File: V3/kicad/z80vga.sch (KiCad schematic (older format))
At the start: 0 parts

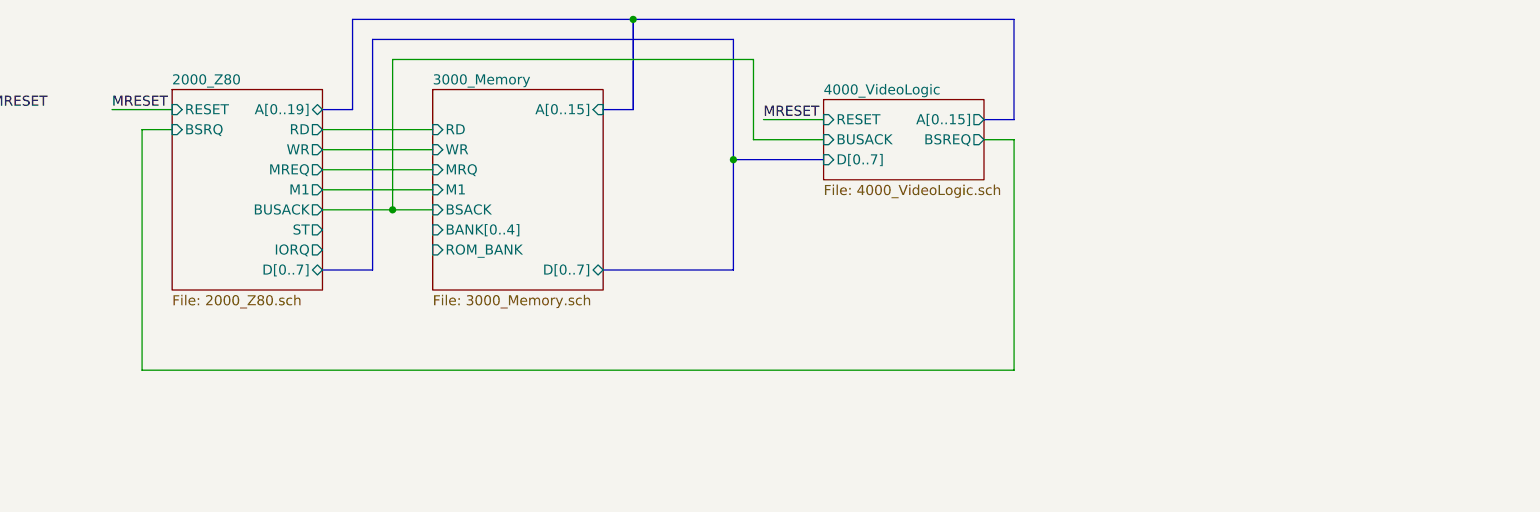
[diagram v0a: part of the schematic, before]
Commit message: probably going to split into two boards
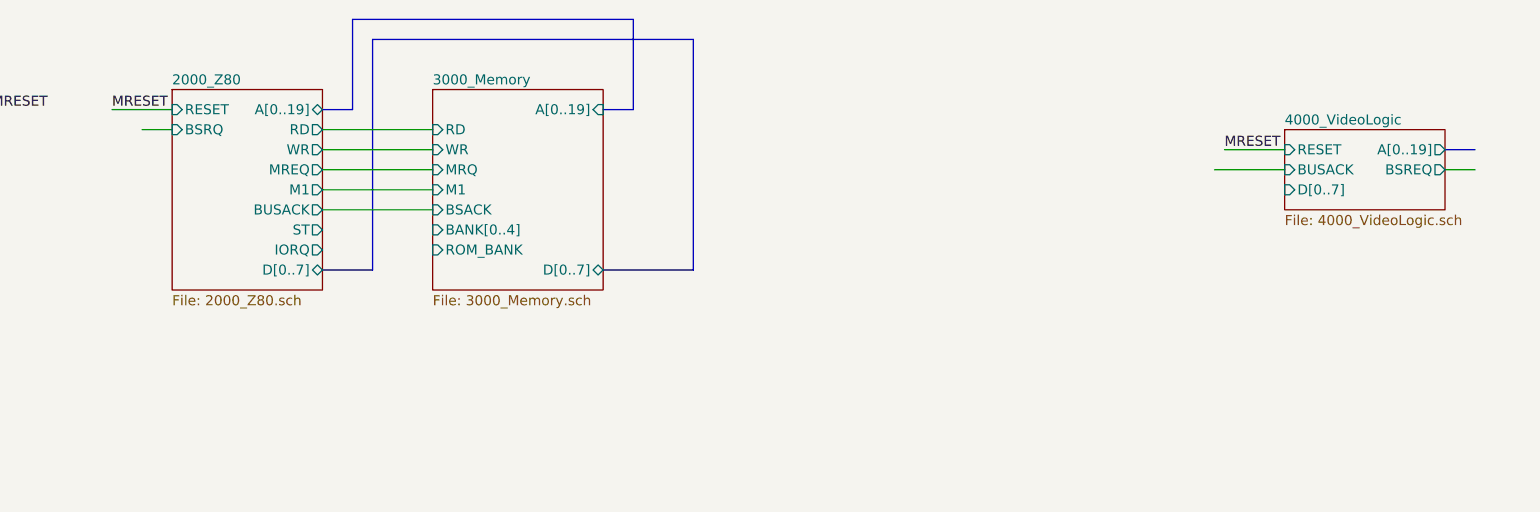
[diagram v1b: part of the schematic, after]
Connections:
- wire segments 18 -> 11
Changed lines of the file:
@@
 $Descr A3 16535 11693
 encoding utf-8
-Sheet 1 16
+Sheet 1 7
 Title ""
 Date ""
@@
 Text Label 6500 5000 0    50   ~ 0
 MRESET
-$Sheet
-S 10050 4950 800  400
-U 61E50944
-F0 "4000_VideoLogic" 50
-F1 "4000_VideoLogic.sch" 50
-F2 "RESET" I L 10050 5050 50
-F3 "BUSACK" I L 10050 5150 50
-F4 "A[0..15]" O R 10850 5050 50
-F5 "D[0..7]" I L 10050 5250 50
-F6 "BSREQ" O R 10850 5150 50
-$EndSheet
 Wire Wire Line
 	7550 5300 8100 5300
@@
 F0 "3000_Memory" 50
 F1 "3000_Memory.sch" 50
-F2 "A[0..15]" I R 8950 5000 50
-F3 "MRQ" I L 8100 5300 50
-F4 "RD" I L 8100 5100 50
-F5 "M1" I L 8100 5400 50
-F6 "BSACK" I L 8100 5500 50
-F7 "WR" I L 8100 5200 50
-F8 "BANK[0..4]" I L 8100 5600 50
-F9 "ROM_BANK" I L 8100 5700 50
-F10 "D[0..7]" B R 8950 5800 50
+F2 "MRQ" I L 8100 5300 50
+F3 "RD" I L 8100 5100 50
+F4 "M1" I L 8100 5400 50
+F5 "BSACK" I L 8100 5500 50
+F6 "WR" I L 8100 5200 50
+F7 "BANK[0..4]" I L 8100 5600 50
+F8 "ROM_BANK" I L 8100 5700 50
+F9 "D[0..7]" B R 8950 5800 50
+F10 "A[0..19]" I R 8950 5000 50
 $EndSheet
 Wire Wire Line
@@
 Wire Bus Line
 	8950 5000 9100 5000
+Wire Bus Line
+	13300 5200 13150 5200
 Wire Wire Line
-	10050 5050 9750 5050
-Text Label 9750 5050 0    50   ~ 0
-MRESET
-Wire Bus Line
-	11000 5050 10850 5050
-Wire Wire Line
-	10850 5150 11000 5150
-Wire Wire Line
-	11000 5150 11000 6300
-Wire Wire Line
-	11000 6300 6650 6300
-Wire Wire Line
-	6650 6300 6650 5100
+	13150 5300 13300 5300
 Wire Wire Line
 	6650 5100 6800 5100
@@
 Wire Bus Line
 	9100 4550 9100 5000
-Connection ~ 9100 4550
-Wire Bus Line
-	9100 4550 11000 4550
-Wire Bus Line
-	11000 4550 11000 5050
 Wire Bus Line
 	7800 5800 7800 4650
 Wire Bus Line
-	7800 4650 9600 4650
-Wire Bus Line
-	9600 4650 9600 5250
-Wire Bus Line
-	9600 5250 10050 5250
-Wire Bus Line
-	9600 5250 9600 5800
-Connection ~ 9600 5250
+	7800 4650 9400 4650
 Wire Bus Line
 	7550 5800 7800 5800
 Wire Bus Line
-	8950 5800 9600 5800
+	8950 5800 9400 5800
+Wire Bus Line
+	9400 4650 9400 5800
 Wire Wire Line
-	7550 5500 7900 5500
+	7550 5500 8100 5500
 Wire Wire Line
-	9700 5150 10050 5150
+	12000 5300 12350 5300
+Text Label 12050 5200 0    50   ~ 0
+MRESET
 Wire Wire Line
-	9700 5150 9700 4750
-Wire Wire Line
-	9700 4750 7900 4750
-Wire Wire Line
-	7900 4750 7900 5500
-Connection ~ 7900 5500
-Wire Wire Line
-	7900 5500 8100 5500
+	12350 5200 12050 5200
+$Sheet
+S 12350 5100 800  400
+U 61E50944
+F0 "4000_VideoLogic" 50
+F1 "4000_VideoLogic.sch" 50
+F2 "RESET" I L 12350 5200 50
+F3 "BUSACK" I L 12350 5300 50
+F4 "D[0..7]" I L 12350 5400 50
+F5 "BSREQ" O R 13150 5300 50
+F6 "A[0..19]" O R 13150 5200 50
+$EndSheet
 $EndSCHEMATC

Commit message: Updated PCB files
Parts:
- added C1000: .33uF, Capacitor_THT:CP_Radial_D5.0mm_P2.00mm, symbol Device:CP1
- added C1001: >.1uF, Capacitor_THT:CP_Radial_D5.0mm_P2.00mm, symbol Device:CP1
- added D1000: 1N4001, Diode_THT:D_DO-41_SOD81_P10.16mm_Horizontal, symbol Diode:1N4001
- added H0, H1, H2, H3: MountingHole, MountingHole:MountingHole_3.5mm, symbol Mechanical:MountingHole
- added J1000: Barrel_Jack_Switch, Connector_BarrelJack:BarrelJack_Horizontal, symbol Connector:Barrel_Jack_Switch
- added U1000: L7805, Package_TO_SOT_SMD:TO-263-3_TabPin2, symbol Regulator_Linear:L7805
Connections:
- net labels added: +5V, GND
- net labels removed: MRESET
- wire segments 11 -> 15
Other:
- note added: "This page has been checked!"

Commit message: Hopefully the last major changes to the CPU
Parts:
- added D1000: LED, LED_THT:LED_D3.0mm, symbol Device:LED
- added R1000: 2.2K, Resistor_THT:R_Axial_DIN0309_L9.0mm_D3.2mm_P2.54mm_Vertical, symbol Device:R
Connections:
- net +5V: now also R1000.2
- net GND: now also D1000.1 (K)
- new net: D1000.2 (A), R1000.1
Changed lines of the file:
@@
 	1    0    0    -1
 $EndComp
+$Comp
+L Device:LED D?
+U 1 1 62A5A6D1
+P 7700 6050
+AR Path="/6191B6A2/61EBDADB/62A5A6D1" Ref="D?"  Part="1"
+AR Path="/62A5A6D1" Ref="D1000"  Part="1"
+F 0 "D1000" H 7700 6200 50  0000 C TNN
+F 1 "LED" H 7700 5950 50  0000 C CNN
+F 2 "LED_THT:LED_D3.0mm" H 7700 6050 50  0001 C CNN
+F 3 "~" H 7700 6050 50  0001 C CNN
+	1    7700 6050
+	-1   0    0    1
+$EndComp
+$Comp
+L power:GND #PWR?
+U 1 1 62A5A6D8
+P 7850 6050
+AR Path="/6191B6A2/61EBDADB/62A5A6D8" Ref="#PWR?"  Part="1"
+AR Path="/62A5A6D8" Ref="#PWR?"  Part="1"
+F 0 "#PWR?" H 7850 5800 50  0001 C CNN
+F 1 "GND" V 7855 5922 50  0000 R CNN
+F 2 "" H 7850 6050 50  0001 C CNN
+F 3 "" H 7850 6050 50  0001 C CNN
+	1    7850 6050
+	0    -1   -1   0
+$EndComp
+$Comp
+L power:+5V #PWR?
+U 1 1 62A5BC7A
+P 7250 6050
+F 0 "#PWR?" H 7250 5900 50  0001 C CNN
+F 1 "+5V" V 7265 6178 50  0000 L CNN
+F 2 "" H 7250 6050 50  0001 C CNN
+F 3 "" H 7250 6050 50  0001 C CNN
+	1    7250 6050
+	0    -1   -1   0
+$EndComp
+$Comp
+L Device:R R?
+U 1 1 62A654EB
+P 7400 6050
+AR Path="/6191B6A2/61EBDADB/62542978/62A654EB" Ref="R?"  Part="1"
+AR Path="/62A654EB" Ref="R1000"  Part="1"
+F 0 "R1000" V 7500 5900 50  0000 L CNN
+F 1 "2.2K" V 7300 5950 50  0000 L CNN
+F 2 "Resistor_THT:R_Axial_DIN0309_L9.0mm_D3.2mm_P2.54mm_Vertical" V 7330 6050 50  0001 C CNN
+F 3 "~" H 7400 6050 50  0001 C CNN
+	1    7400 6050
+	0    1    1    0
+$EndComp
 $EndSCHEMATC
